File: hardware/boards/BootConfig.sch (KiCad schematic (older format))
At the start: 33 parts, among them J3 Conn_02x05_Odd_Even, Q6 Q_NMOS_GSD, SW1 SW_DIP_x03, SW2 RESET, U1 ECP5UM5G-381caBGA, U3 CYUSB3014, U5 128MiB, Y1 19.2MHz

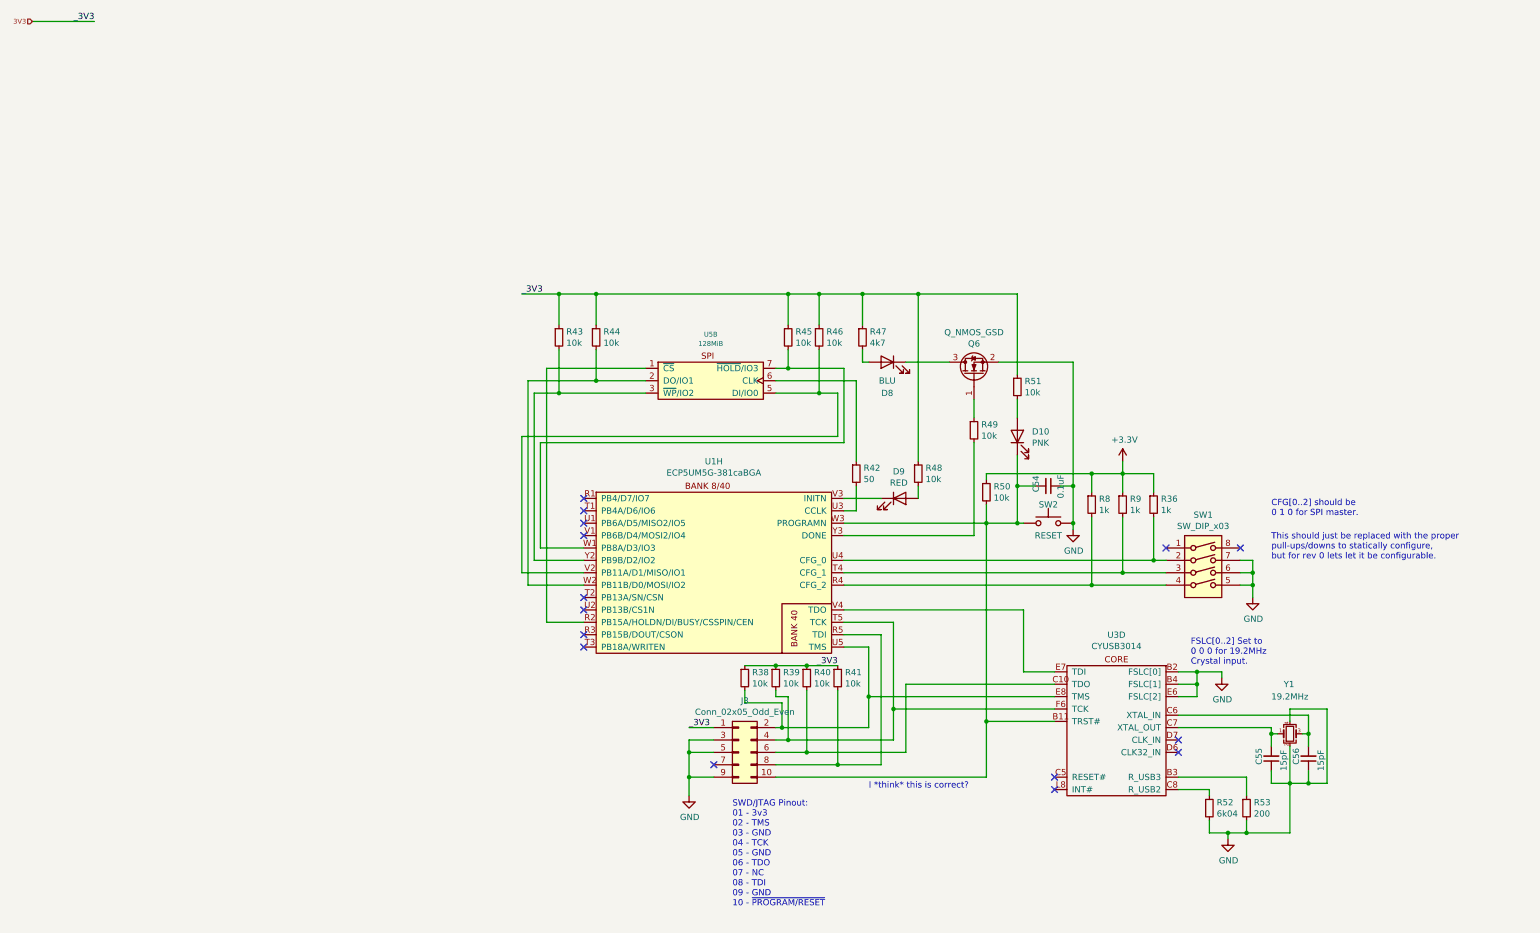
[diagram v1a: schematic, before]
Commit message: Resized some nested schematics and pulled the GPIF II interrupt line out from the boot config block into the USB 3 interface
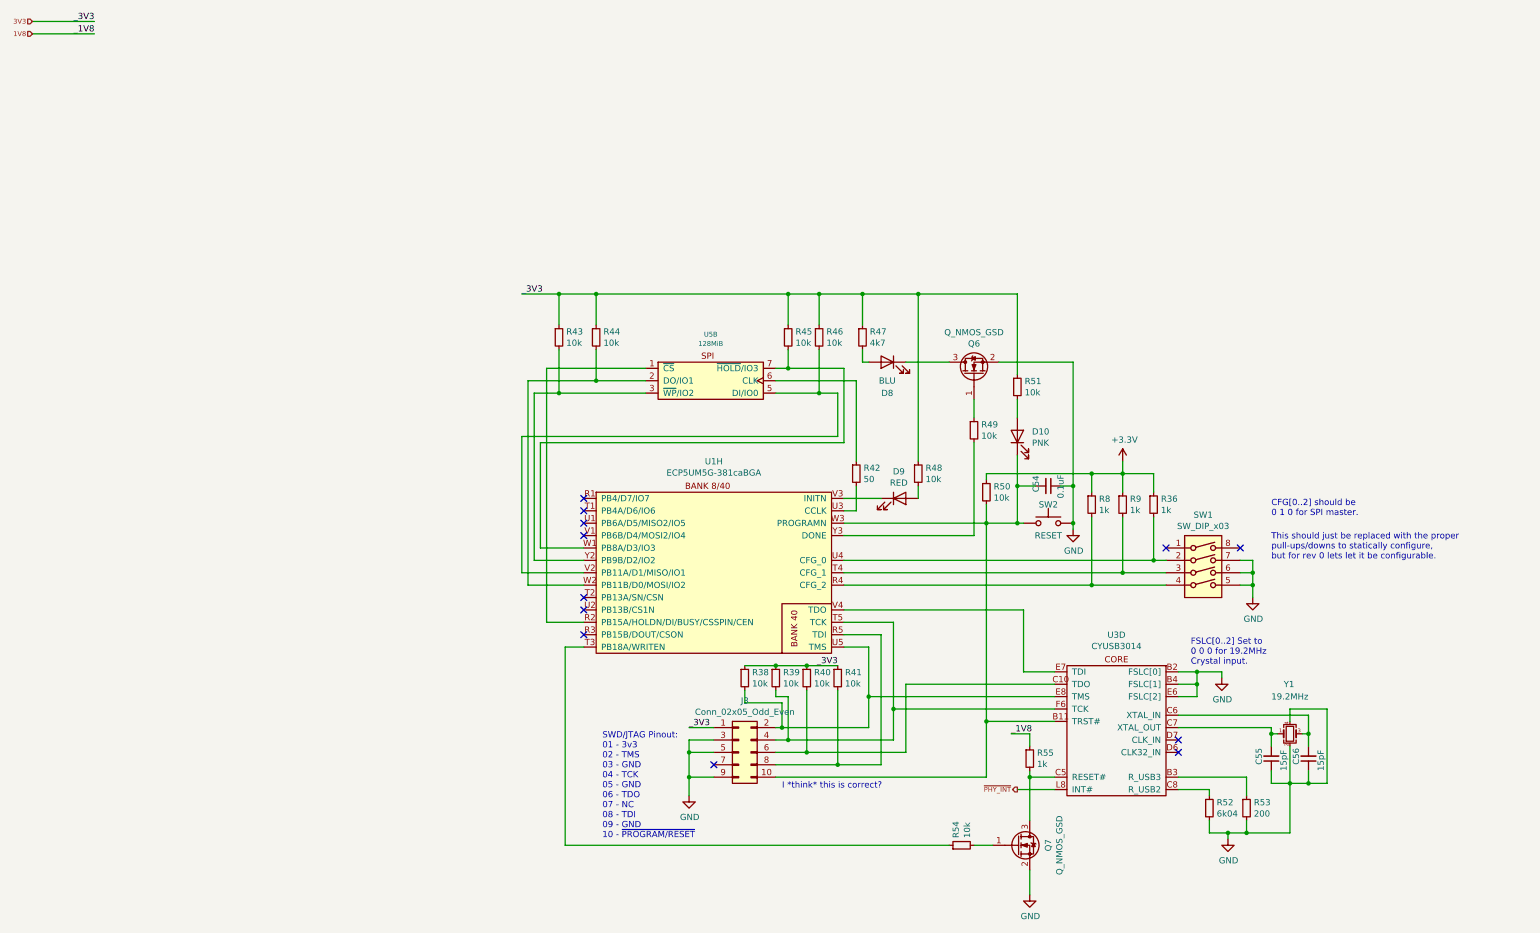
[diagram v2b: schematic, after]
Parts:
- added Q7: Q_NMOS_GSD, Package_TO_SOT_SMD:SOT-23, symbol Device:Q_NMOS_GSD
- added R54: 10k, Resistor_SMD:R_0603_1608Metric, symbol Device:R_Small
- added R55: 1k, Resistor_SMD:R_0603_1608Metric, symbol Device:R_Small
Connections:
- net GND: now also Q7.2 (S)
- net at U1.T3 (PB18A/WRITEN): now also R54.1
- net at U3.C5 (RESET#): now also Q7.3 (D), R55.2
- net ~PHY_INT: now reaches U3.L8 (INT#)
- new net: Q7.1 (G), R54.2
- new net 1V8: R55.1
- no-connect marks 15 -> 12
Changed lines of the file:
@@
 $Descr A3 16535 11693
 encoding utf-8
-Sheet 11 11
+Sheet 10 11
 Title "lethallink"
 Date "2020-06-13"
@@
 NoConn ~ 5200 5350
 NoConn ~ 5200 5550
-NoConn ~ 5200 5650
 Wire Wire Line
 	7300 4950 9800 4950
@@
 NoConn ~ 10000 6400
 NoConn ~ 10000 6500
-NoConn ~ 9000 6800
-NoConn ~ 9000 6700
 $Comp
 L lethalbit:CYUSB3014 U?
@@
 Wire Wire Line
 	8450 6700 8450 6250
-Text Notes 7500 6800 0    50   ~ 0
+Text Notes 6800 6800 0    50   ~ 0
 I *think* this is correct?
 Wire Wire Line
@@
 Text Label 6050 6300 0    50   ~ 0
 _3V3
-Text Notes 6400 7750 0    50   ~ 0
+Text Notes 5350 7200 0    50   ~ 0
 SWD/JTAG Pinout:\n01 - 3v3\n02 - TMS\n03 - GND\n04 - TCK\n05 - GND\n06 - TDO\n07 - NC\n08 - TDI\n09 - GND\n10 - ~PROGRAM/RESET
 Wire Wire Line
@@
 Text Notes 10100 5800 0    50   ~ 0
 FSLC[0..2] Set to\n0 0 0 for 19.2MHz\nCrystal input.\n
+Text HLabel 750  700  0    39   Input ~ 0
+1V8
+Wire Wire Line
+	750  700  1250 700
+Text Label 1250 700  2    50   ~ 0
+_1V8
+$Comp
+L Device:Q_NMOS_GSD Q?
+U 1 1 60A975BF
+P 8700 7250
+AR Path="/5EDF9F51/60A975BF" Ref="Q?"  Part="1"
+AR Path="/5EF66251/60A975BF" Ref="Q7"  Part="1"
+F 0 "Q7" V 8949 7250 50  0000 C CNN
+F 1 "Q_NMOS_GSD" V 9040 7250 50  0000 C CNN
+F 2 "Package_TO_SOT_SMD:SOT-23" H 8900 7350 50  0001 C CNN
+F 3 "~" H 8700 7250 50  0001 C CNN
+F 4 "Diodes Incorporated" V 8700 7250 50  0001 C CNN "MFR"
+F 5 "DMN65D8L-7" V 8700 7250 50  0001 C CNN "MPN"
+	1    8700 7250
+	1    0    0    -1
+$EndComp
+Wire Wire Line
+	8800 6700 9000 6700
+Wire Wire Line
+	8800 6700 8800 7050
+Connection ~ 8800 6700
+$Comp
+L power:GND #PWR0136
+U 1 1 60AE0264
+P 8800 7650
+F 0 "#PWR0136" H 8800 7400 50  0001 C CNN
+F 1 "GND" H 8805 7477 50  0000 C CNN
+F 2 "" H 8800 7650 50  0001 C CNN
+F 3 "" H 8800 7650 50  0001 C CNN
+	1    8800 7650
+	1    0    0    -1
+$EndComp
+Wire Wire Line
+	8800 7450 8800 7650
+Wire Wire Line
+	8800 6650 8800 6700
+Wire Wire Line
+	8800 6450 8800 6350
+Wire Wire Line
+	8800 6350 8650 6350
+Text Label 8650 6350 0    50   ~ 0
+_1V8
+$Comp
+L Device:R_Small R?
+U 1 1 60B3741A
+P 8250 7250
+AR Path="/5EDF9F51/60B3741A" Ref="R?"  Part="1"
+AR Path="/5EF66251/60B3741A" Ref="R54"  Part="1"
+F 0 "R54" H 8309 7296 50  0000 L CNN
+F 1 "10k" H 8309 7205 50  0000 L CNN
+F 2 "Resistor_SMD:R_0603_1608Metric" H 8250 7250 50  0001 C CNN
+F 3 "~" H 8250 7250 50  0001 C CNN
+F 4 "Vishay Dale" H 8250 7250 50  0001 C CNN "MFR"
+F 5 "CRCW060310K0FKEA" H 8250 7250 50  0001 C CNN "MPN"
+	1    8250 7250
+	0    -1   -1   0
+$EndComp
+Wire Wire Line
+	8350 7250 8500 7250
+Wire Wire Line
+	5200 5650 5050 5650
+Wire Wire Line
+	5050 5650 5050 7250
+Wire Wire Line
+	5050 7250 8150 7250
+$Comp
+L Device:R_Small R55
+U 1 1 60BACCCC
+P 8800 6550
+F 0 "R55" H 8859 6596 50  0000 L CNN
+F 1 "1k" H 8859 6505 50  0000 L CNN
+F 2 "Resistor_SMD:R_0603_1608Metric" H 8800 6550 50  0001 C CNN
+F 3 "~" H 8800 6550 50  0001 C CNN
+F 4 "Vishay Dale" H 8800 6550 50  0001 C CNN "MFR"
+F 5 "CRCW06031K00FKEAHP" H 8800 6550 50  0001 C CNN "MPN"
+	1    8800 6550
+	1    0    0    -1
+$EndComp
+Text HLabel 8700 6800 0    39   Output ~ 0
+~PHY_INT
+Wire Wire Line
+	8700 6800 9000 6800
 $EndSCHEMATC

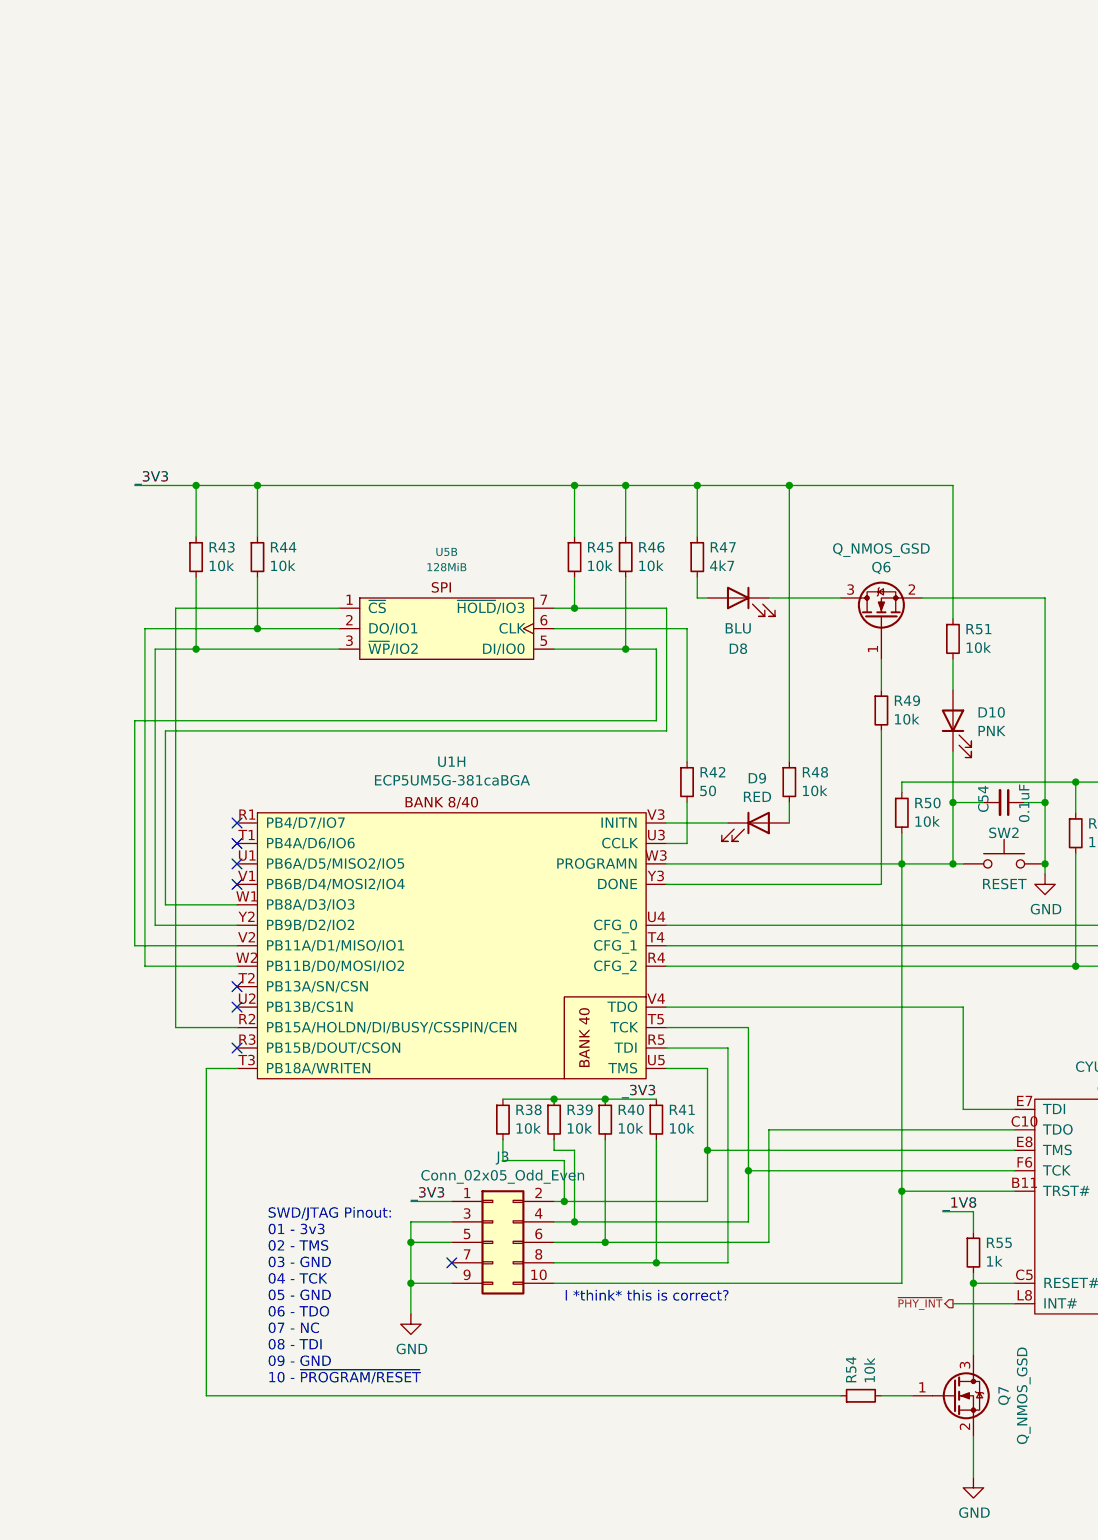
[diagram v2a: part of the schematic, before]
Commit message: Added headers for the SPI flash for both the FPGA and the PHY
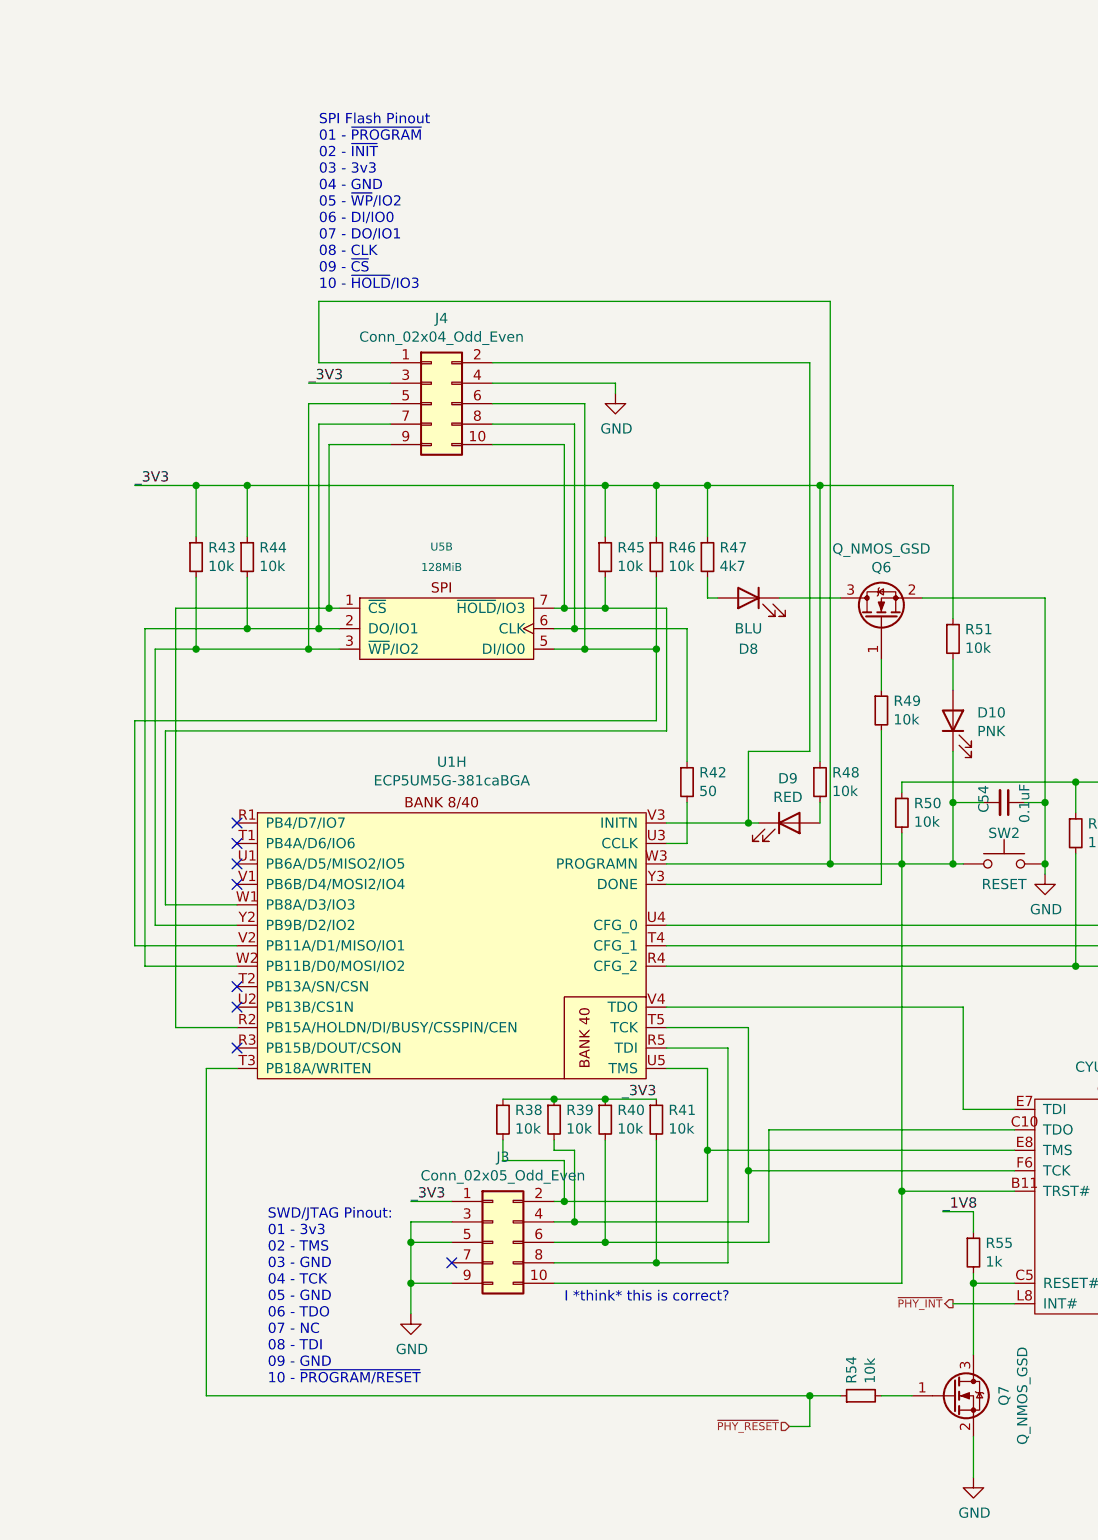
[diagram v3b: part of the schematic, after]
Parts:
- added J4: Conn_02x04_Odd_Even, Connector_PinHeader_1.27mm:PinHeader_2x05_P1.27mm_Vertical, symbol Connector_Generic:Conn_02x05_Odd_Even
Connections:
- net 3V3: now also J4.3 (Pin_3)
- net GND: now also J4.4 (Pin_4)
- net at U1.R2 (PB15A/HOLDN/DI/BUSY/CSSPIN/CEN), U5.1 (~CS): now also J4.9 (Pin_9)
- net at R44.2, U1.W2 (PB11B/D0/MOSI/IO2), U5.2 (DO/IO1): now also J4.7 (Pin_7)
- net at R43.2, U1.Y2 (PB9B/D2/IO2), U5.3 (~WP~/IO2): now also J4.5 (Pin_5)
- net at R46.2, U1.V2 (PB11A/D1/MISO/IO1), U5.5 (DI/IO0): now also J4.6 (Pin_6)
- net at R42.1, U5.6 (CLK): now also J4.8 (Pin_8)
- net at R45.2, U1.W1 (PB8A/D3/IO3), U5.7 (~HOLD~/IO3): now also J4.10 (Pin_10)
- net ~PHY_RESET: now reaches R54.1, U1.T3 (PB18A/WRITEN)
- net at D9.1 (K), U1.V3 (INITN): now also J4.2 (Pin_2)
- net at C54.2, D10.1 (K), J3.10 (Pin_10)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: now also J4.1 (Pin_1)
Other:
- note added: "SPI Flash Pinout\n01 - ~PROGRAM~\n02 - ~INIT~\n03 - 3v3\n04 - GND\n05 - ~WP~/IO2\n06 - DI/IO0\n07 - DO/IO1\n08 - CLK\n09 - ~CS~\n10 - ~HOLD~/IO3\n"
- moved on the sheet: D8, D9, R44, R45, R46, R47, R48

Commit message: A batch of misc changes, I don't exactly recall what changed
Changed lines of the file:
@@
 	5200 5050 4700 5050
 Wire Wire Line
-	4700 5050 4700 3950
-Wire Wire Line
 	4700 3950 7250 3950
 Wire Wire Line
@@
 Wire Wire Line
 	5200 5150 4750 5150
-Wire Wire Line
-	4750 3500 4750 5150
 NoConn ~ 5200 4750
 NoConn ~ 5200 4650
@@
 	5200 4950 4800 4950
 Wire Wire Line
-	4800 4950 4800 3600
-Wire Wire Line
 	5200 4850 4850 4850
 Wire Wire Line
-	4850 4850 4850 4000
-Wire Wire Line
 	4850 4000 7300 4000
 Wire Wire Line
@@
 Wire Wire Line
 	5200 5450 4900 5450
-Wire Wire Line
-	4900 5450 4900 3400
 Wire Wire Line
 	4900 3400 5650 3400
@@
 Wire Wire Line
 	7250 3050 7250 2800
-Wire Wire Line
-	7400 4150 7400 3500
 $Comp
 L Device:R_Small R42
@@
 Wire Wire Line
 	8000 7250 8150 7250
+Wire Wire Line
+	4900 3400 4900 5450
+Wire Wire Line
+	7400 3500 7400 4150
+Wire Wire Line
+	4700 3950 4700 5050
+Wire Wire Line
+	4750 3500 4750 5150
+Wire Wire Line
+	4850 4000 4850 4850
+Wire Wire Line
+	4800 3600 4800 4950
 $EndSCHEMATC

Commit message: Some messing about with the GPIF interface
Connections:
- net TDI: now reaches J3.8 (Pin_8), R41.2, U1.R5 (TDI)
- net TCK: now reaches J3.4 (Pin_4), R39.2, U1.T5 (TCK), U3.F6 (TCK)
- net TMS: now reaches J3.2 (Pin_2), R38.2, U1.U5 (TMS), U3.E8 (TMS)
- net ~INIT: now reaches D9.1 (K), J4.2 (Pin_2), U1.V3 (INITN)
- net TDO: now reaches U1.V4 (TDO), U3.E7 (TDI)
- net ~RESET: now reaches C54.2, D10.1 (K), J3.10 (Pin_10), J4.1 (Pin_1), R50.2, SW2.1, U1.W3 (PROGRAMN), U3.B11 (TRST#)
- net DONE: now reaches R49.2, U1.Y3 (DONE)
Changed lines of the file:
@@
 Wire Wire Line
 	4800 3600 4800 4950
+Text Label 7350 5350 0    50   ~ 0
+TDO
+Text Label 7350 5450 0    50   ~ 0
+TCK
+Text Label 7350 5550 0    50   ~ 0
+TDI
+Text Label 7350 5650 0    50   ~ 0
+TMS
+Text Label 6800 6700 0    50   ~ 0
+~RESET
+Text Label 7750 4100 0    50   ~ 0
+~INIT
+Text Label 7400 4750 0    50   ~ 0
+DONE
 $EndSCHEMATC
